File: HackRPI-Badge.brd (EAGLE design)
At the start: 101.6 x 71.1 mm, 24 parts, among them IC1 74595, IC2 74595, IC3 74595

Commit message: Moved resistor nets to ensure constant LED brightness, added serial connector, added 74HC165 for input
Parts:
- removed R7: 10k, SparkFun-Resistors:0603-RES
- removed R8: 470, SparkFun-Resistors:0603-RES
- removed RESET: (no value), SparkFun-Electromechanical:TACTILE-SWITCH-SMD
- added C5: .1uF, SparkFun-Capacitors:0603-CAP
- added J1: FTDI_BASICPTH, SparkFun-Connectors:FTDI_BASIC
- added J2: SOLDERJUMPERTRACE-PTH, SparkFun-Retired:SJ_2S-TRACE-PTH
- added RN1, RN2, RN3, RN4: 47, SparkFun-Passives:0603-ARV
- added U$1: 74165DT, mylib:TSSOP16
- R2, R3: value 47 -> 10k; device SparkFun-Passives:0603-ARV -> SparkFun-Resistors:0603-RES
- R6: value 10k -> 470
- moved R2 24.2 mm to (-50.8, -38.1)
- moved R3 21.6 mm to (-50.8, -41.9)
- moved R5 14.0 mm to (-50.8, -55.9)
- moved R6 14.0 mm to (-50.8, -59.7)
- moved R4 7.62 mm to (-50.8, -45.7)
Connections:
- new net DTR: C5.2, J1.DTR
- new net N$1: J2.1, R6.2
- new net N$10: LED_LEFT.6, RN2.1
- new net N$11: LED_LEFT.11, RN2.2
- new net N$3: LED_LEFT.13, RN1.1
- new net N$4: LED_LEFT.3, RN1.2
- new net N$8: LED_LEFT.4, RN1.3
- new net N$9: LED_LEFT.10, RN1.4
- new net RXI: J1.TXO, WIFI.15
- new net TXO: J1.RXI, WIFI.16
- new net VCC: U$1.16
- net 3.3V: now also R3.2, R4.2; no longer R6.2, R7.2
- net C0: now also RN1.8; no longer LED_LEFT.13
- net C1: now also RN1.7; no longer LED_LEFT.3
- net C10: now also RN3.6; no longer LEF_RIGHT.4
- net C11: now also RN3.5; no longer LEF_RIGHT.10
- net C12: now also RN4.8; no longer LEF_RIGHT.6
- net C13: now also RN4.7; no longer LEF_RIGHT.11
- net C14: now also RN4.6; no longer LEF_RIGHT.15
- net C15: now also RN4.5; no longer LEF_RIGHT.16
- net C2: now also RN1.6; no longer LED_LEFT.4
- net C3: now also RN1.5; no longer LED_LEFT.10
- net C4: now also RN2.8; no longer LED_LEFT.6
- net C5: now also RN2.7; no longer LED_LEFT.11
- net C6: now also RN2.6; no longer LED_LEFT.15
- net C7: now also RN2.5; no longer LED_LEFT.16
- net C8: now also RN3.8; no longer LEF_RIGHT.13
- net C9: now also RN3.7; no longer LEF_RIGHT.3
- net GND: now also J1.GND, R2.2, U$1.8; no longer R4.2, RESET.1
- net GPIO0: now also R3.1; no longer R5.1
- net GPIO15: now also R2.1; no longer R4.1
- net GPIO16: now also J2.2; no longer R8.2
- net GPIO2: now also R4.1; no longer R6.1
- net N$12: now also LED_LEFT.15, RN2.3; no longer WIFI.15
- net N$13: now also LED_LEFT.16, RN2.4; no longer WIFI.16
- net N$14: now also ULN1.17; no longer R2.7
- net N$15: now also ULN1.16; no longer R2.6
- net N$16: now also ULN1.15; no longer R2.5
- net N$17: now also ULN1.14; no longer R3.8
- net N$18: now also ULN1.13; no longer R3.7
- net N$19: now also ULN1.12; no longer R3.6
- net N$20: now also ULN1.11; no longer R3.5
- net N$23: now also LEF_RIGHT.13, RN3.1; no longer R2.1, ULN1.18
- net N$24: now also LEF_RIGHT.3, RN3.2; no longer R2.2, ULN1.17
- net N$25: now also LEF_RIGHT.4, RN3.3; no longer R2.3, ULN1.16
- net N$26: now also LEF_RIGHT.10, RN3.4; no longer R2.4, ULN1.15
- net N$27: now also LEF_RIGHT.6, RN4.1; no longer R3.1, ULN1.14
- net N$28: now also LEF_RIGHT.11, RN4.2; no longer R3.2, ULN1.13
- net N$29: now also LEF_RIGHT.15, RN4.3; no longer R3.3, ULN1.12
- net N$30: now also LEF_RIGHT.16, RN4.4; no longer R3.4, ULN1.11
- net N$7: now also ULN1.18; no longer R2.8
- net RESET: now also C5.1, R5.1, R6.1; no longer R7.1, R8.1, RESET.3

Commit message: Updated part names, misc work
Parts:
- added RN5, RN6: 10k, SparkFun-Passives:0603-ARV
- added S1, S2, S3, S4, S5, S6: SWITCH-MOMENTARY-2PTH, SparkFun-Electromechanical:TACTILE-PTH
- renumbered IC1 to U4, IC2 to U5, IC3 to U6, REG to U2, U$1 to U7, ULN1 to U3, WIFI to U1
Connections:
- removed net VCC: U7.16
- new net A: RN5.1, S1.3, U7.11
- new net B: RN5.2, S2.3, U7.12
- new net CLK: U7.2
- new net DOWN: RN6.2, S6.3, U7.4
- new net LEFT: RN5.3, S3.3, U7.13
- new net RIGHT: RN6.1, S5.3, U7.3
- new net UP: RN5.4, S4.3, U7.14
- net 3.3V: now also RN5.5, RN5.6, RN5.7, RN5.8, RN6.7, RN6.8, U7.16
- net GND: now also S1.1, S2.1, S3.1, S4.1, S5.1, S6.1, U7.5, U7.6
- net MISO: now also U7.9
- net OE: now also U7.15

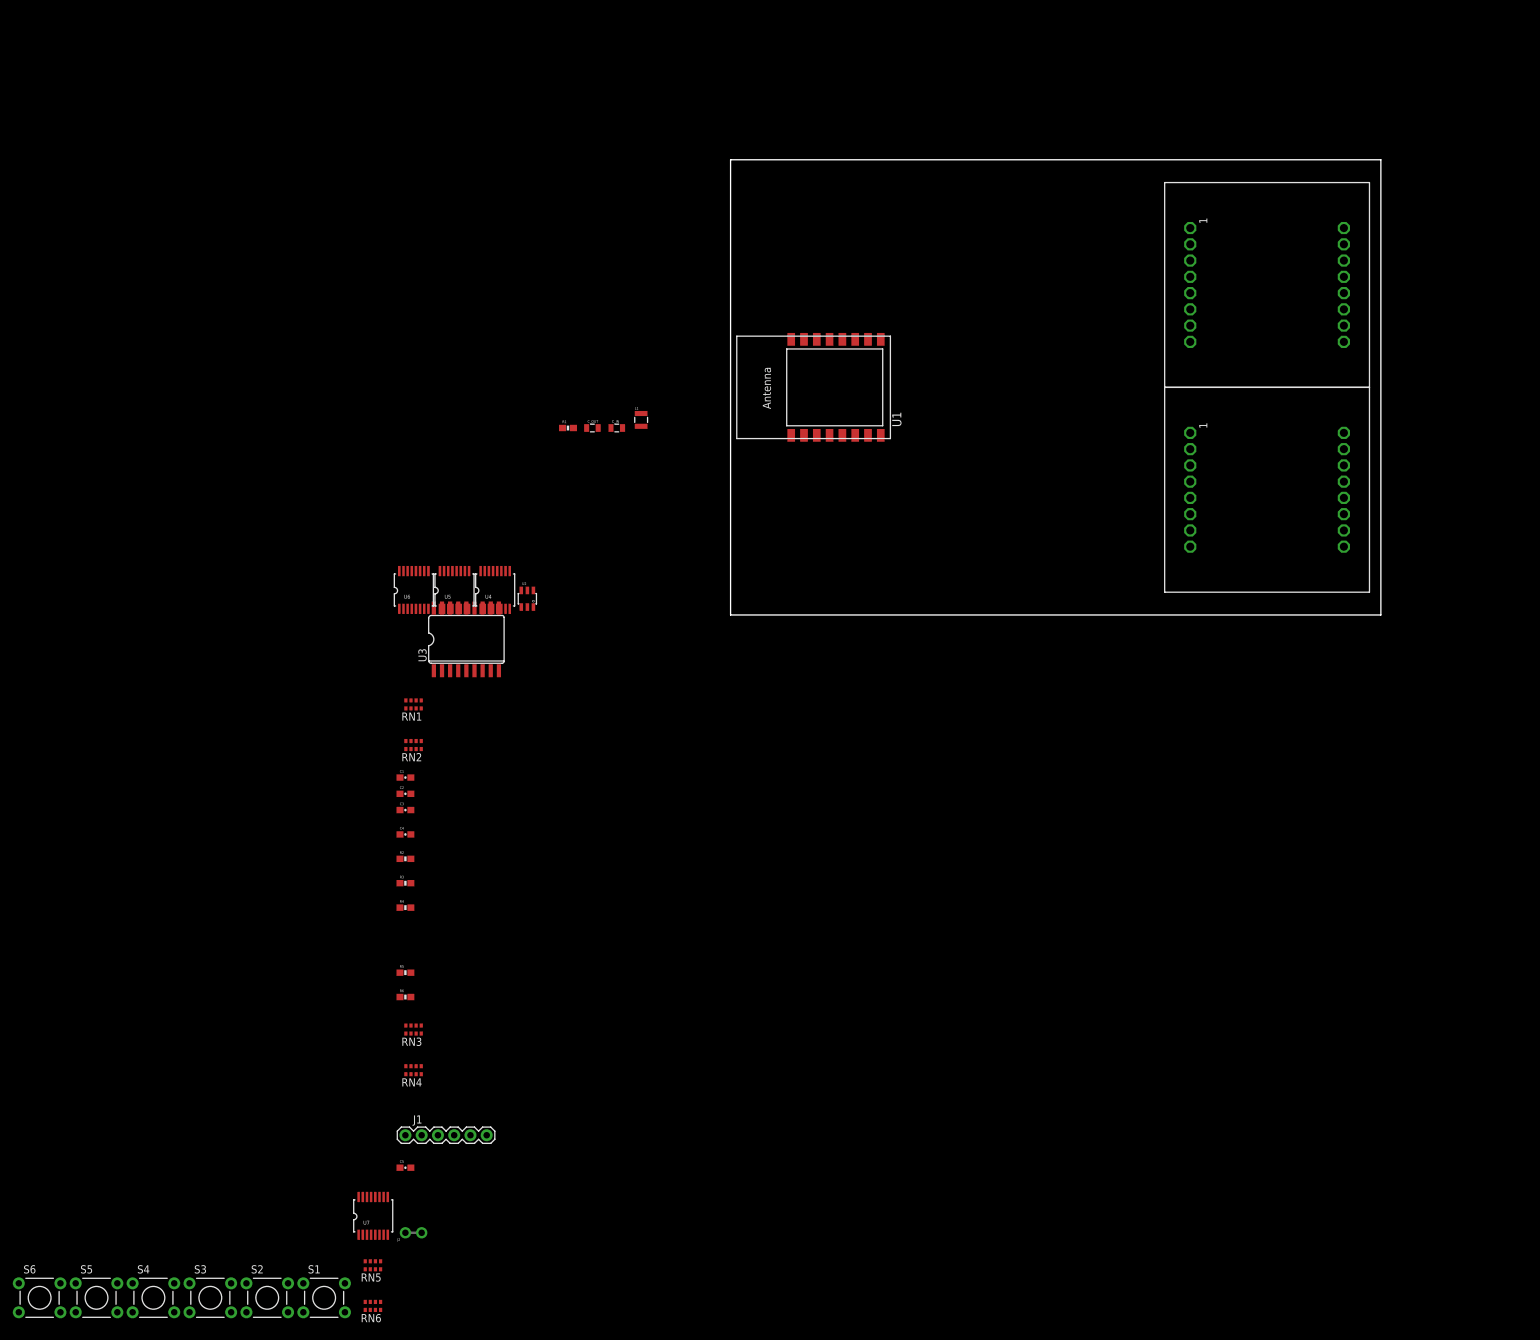
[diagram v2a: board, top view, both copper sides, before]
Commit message: Placed components on board, routed LED matrices and output shift registers, rounded corners of board
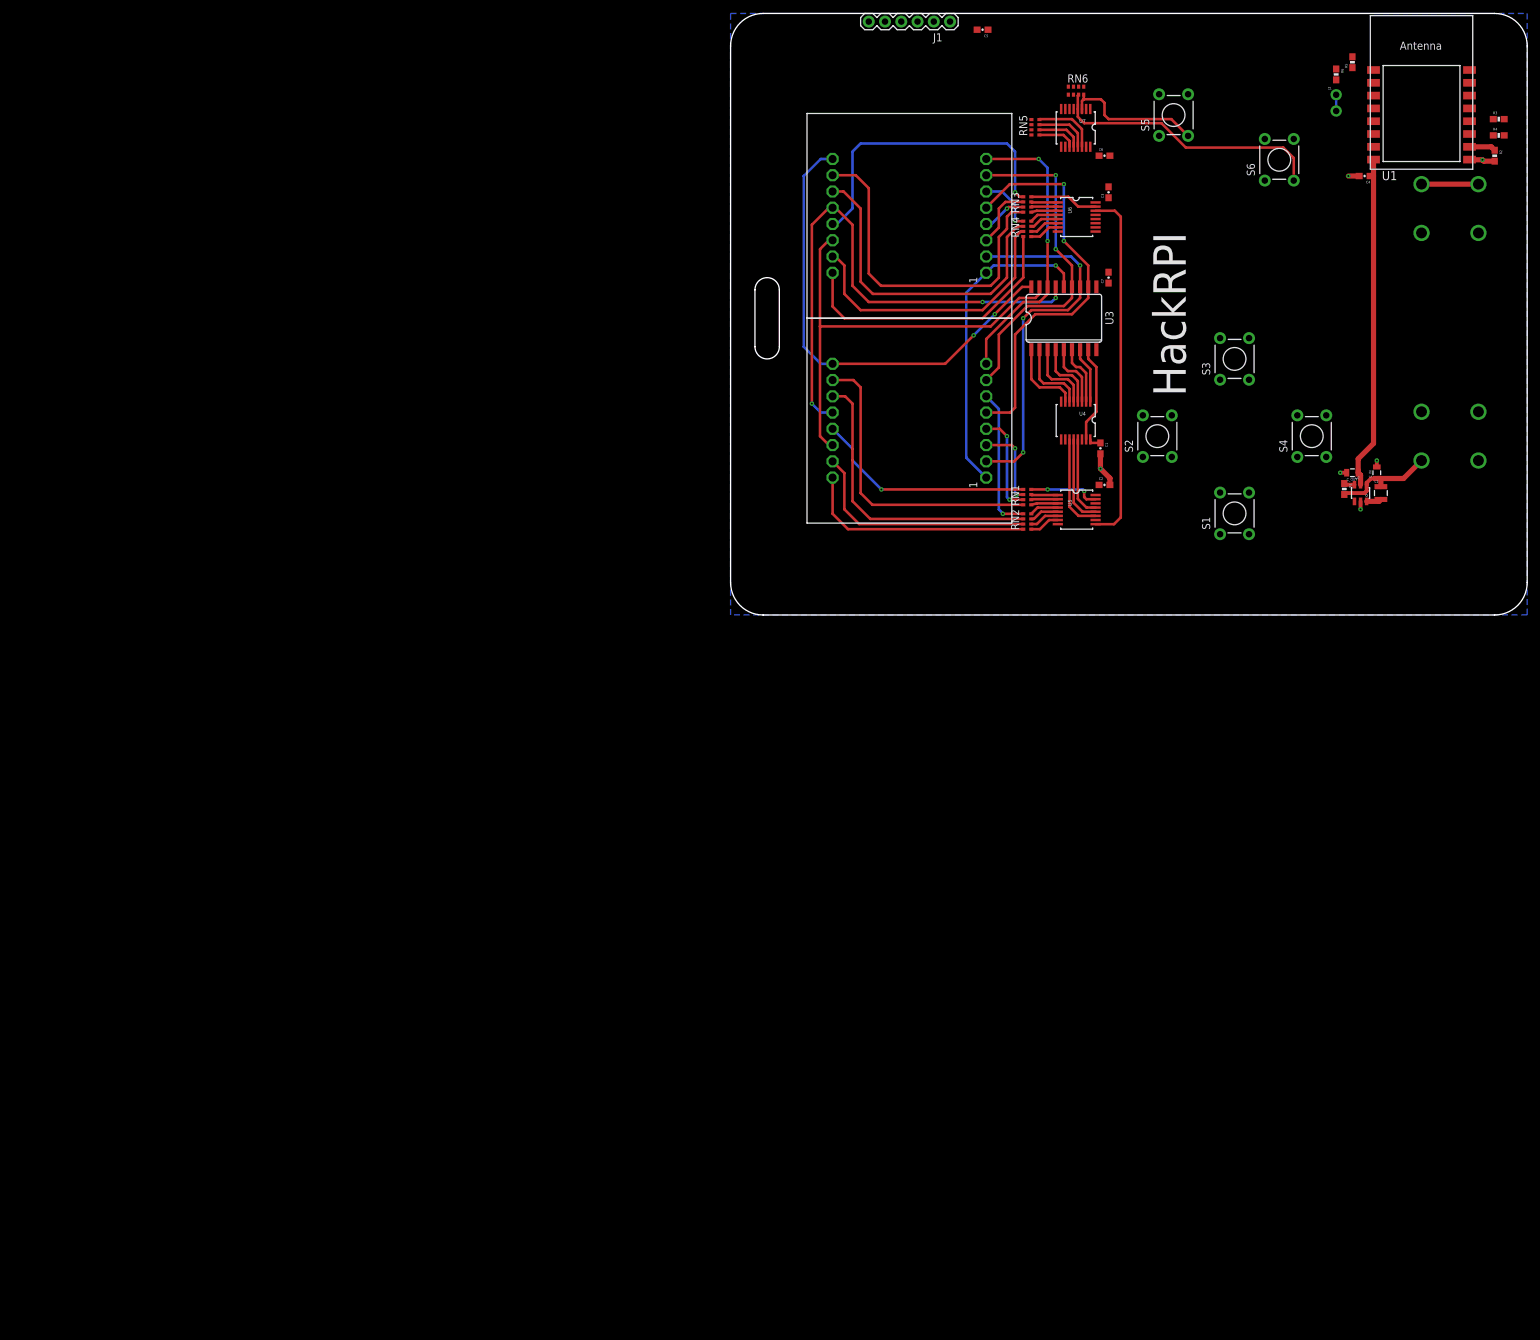
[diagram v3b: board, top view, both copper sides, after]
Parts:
- added BAT1, BAT2: (no value), SparkFun-Electromechanical:BATTERY-AAA
- added C6, C7: .1uF, SparkFun-Capacitors:0603-CAP
- moved S6 262.9 mm to (85.7, 71.1), turned to 90 degrees
- moved S5 249.9 mm to (69.2, 78.1), turned to 90 degrees
- moved J2 227.9 mm to (94.6, 80.0), turned to 270 degrees
- moved S4 225.6 mm to (90.8, 27.9), turned to 90 degrees
- moved RN6 219.4 mm to (54.0, 81.9), turned to 180 degrees
- moved S3 217.1 mm to (78.7, 40.0), turned to 90 degrees
- moved R4 209.1 mm to (120.0, 74.9)
- moved R3 208.4 mm to (120.0, 77.5)
- moved RN5 205.7 mm to (47.6, 76.2), turned to 270 degrees
- moved R5 205.2 mm to (97.2, 86.4), turned to 90 degrees
- moved R6 204.8 mm to (94.6, 84.5), turned to 270 degrees
- moved R2 202.6 mm to (119.4, 71.8), turned to 270 degrees
- moved U7 202.6 mm to (54.0, 76.2), turned to 180 degrees
- moved C5 199.4 mm to (39.4, 91.4), turned to 180 degrees
- moved J1 193.7 mm to (34.3, 92.7), turned to 180 degrees
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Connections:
- new net N$31: BAT1.GND@1, BAT2.PWR@1
- net 3.3V: now also C6.1, C7.1, RN5.1, RN5.2, RN5.3, RN5.4, RN6.1, RN6.2, RN6.3, RN6.4; no longer RN5.5, RN5.6, RN5.7, RN5.8, RN6.7, RN6.8
- net A: now also RN6.8, S5.3, U7.3; no longer RN5.1, S1.3, U7.11
- net B: now also RN6.7, S6.3, U7.4; no longer RN5.2, S2.3, U7.12
- net DOWN: now also RN5.8, S4.3, U7.14; no longer RN6.2, S6.3, U7.4
- net GND: now also BAT2.GND@1, C6.2, C7.2
- net GPIO0: now also U7.1
- net GPIO2: now also U7.15
- net LEFT: now also RN5.5, S1.3, U7.11; no longer RN5.3, S3.3, U7.13
- net OE: no longer U7.15
- net R0: now also U3.8; no longer U3.1
- net R1: now also U3.7; no longer U3.2
- net R2: now also U3.6; no longer U3.3
- net R3: now also U3.5; no longer U3.4
- net R4: now also U3.4; no longer U3.5
- net R5: now also U3.3; no longer U3.6
- net R6: now also U3.2; no longer U3.7
- net R7: now also U3.1; no longer U3.8
- net RIGHT: now also RN5.7, S3.3, U7.13; no longer RN6.1, S5.3, U7.3
- net UP: now also RN5.6, S2.3, U7.12; no longer RN5.4, S4.3, U7.14
- net V_BATT: now also BAT1.PWR@1
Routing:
- net N$16: track 0.00 -> 84.6 mm, vias 0 -> 3
- net N$7: track 0.00 -> 73.9 mm, vias 0 -> 2
- net N$14: track 0.00 -> 71.8 mm
- net N$20: track 0.00 -> 63.1 mm, vias 0 -> 2
- net N$19: track 0.00 -> 57.8 mm, vias 0 -> 3
- net N$22: track 0.00 -> 55.7 mm
- net 3.3V: track 0.00 -> 54.6 mm
- net N$26: track 0.00 -> 54.4 mm
- net N$18: track 0.00 -> 52.8 mm, vias 0 -> 2
- net N$28: track 0.00 -> 51.2 mm
- net N$17: track 0.00 -> 49.8 mm, vias 0 -> 1
- net N$9: track 0.00 -> 47.5 mm
- net N$23: track 0.00 -> 47.4 mm, vias 0 -> 1
- net N$11: track 0.00 -> 46.7 mm
- net N$15: track 0.00 -> 46.2 mm, vias 0 -> 2
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- added copper zone on layer 16, net GND
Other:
- board size 101.6 x 71.1 mm -> 124.5 x 94 mm
- board text added: "HackRPI"

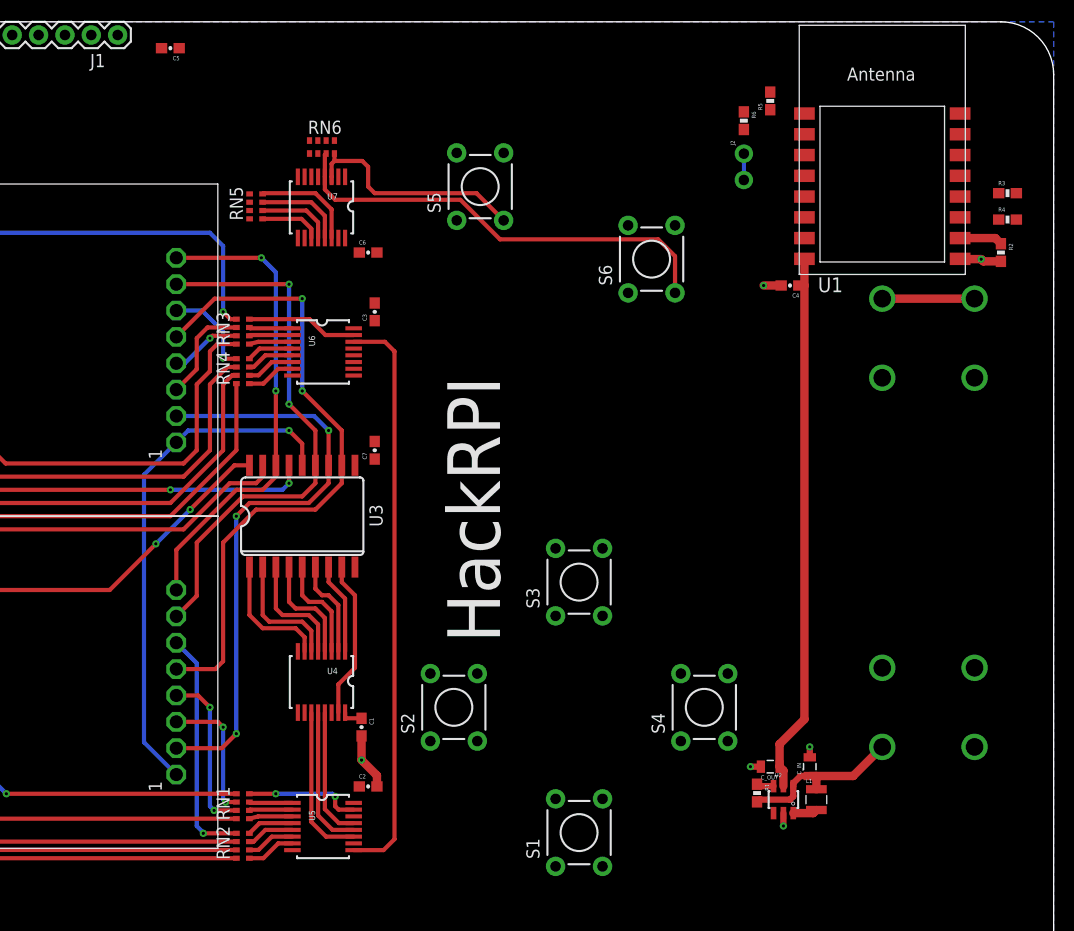
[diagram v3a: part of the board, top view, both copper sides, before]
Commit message: Finished laying out/routing first revision of board
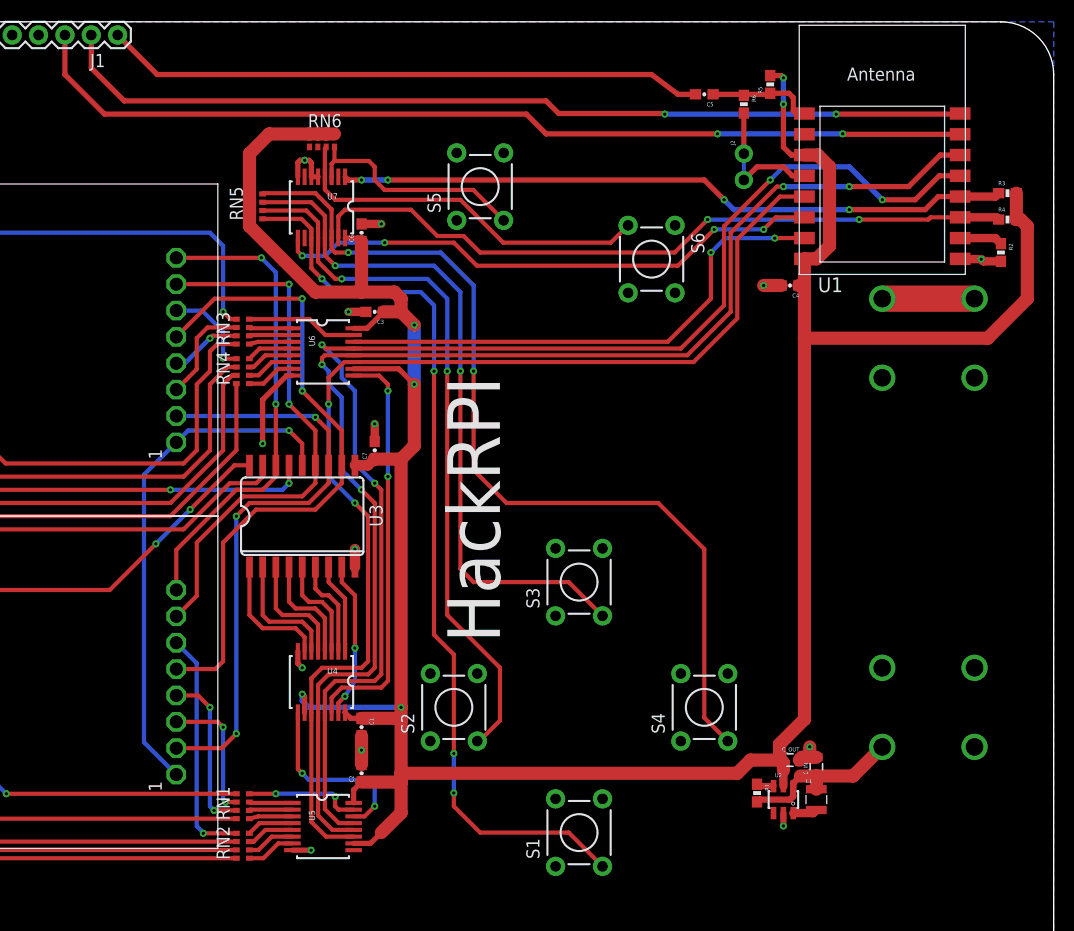
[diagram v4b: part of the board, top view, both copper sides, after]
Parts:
- moved C5 51.6 mm to (90.8, 87.0)
- moved C6 2.01 mm to (57.8, 73.7), turned to 90 degrees
- moved C_OUT 2.01 mm to (99.1, 22.9), turned to 0 degrees
- moved R5 1.59 mm to (97.2, 87.9)
- moved R6 1.59 mm to (94.6, 86.0)
- moved C2 1.42 mm to (57.8, 21.6), turned to 90 degrees
- moved C_IN 0.63 mm to (101.6, 22.2)
- moved RN6 0.63 mm to (54.0, 82.5)
- turned C3 to 180 degrees
- turned S6 to 270 degrees
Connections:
- new net N$33: U5.9
- net MOSI: now also U6.14; no longer U4.14
- net N$22: now also U4.14, U6.9; no longer U5.9, U6.14
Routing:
- net 3.3V: track 54.6 -> 284.5 mm, vias 0 -> 6
- net OE: track 12.6 -> 130.5 mm, vias 0 -> 4
- net LAT: track 13.9 -> 128.7 mm, vias 0 -> 4
- net SCK: track 15.2 -> 111.1 mm, vias 0 -> 2
- net RXI: track 0.00 -> 92.4 mm, vias 0 -> 2
- net TXO: track 0.00 -> 88.7 mm, vias 0 -> 2
- net LEFT: track 5.99 -> 88.0 mm, vias 0 -> 4
- net DOWN: track 10.1 -> 88.9 mm, vias 0 -> 2
- net GPIO2: track 0.00 -> 69.2 mm, vias 0 -> 2
- net GPIO0: track 0.00 -> 64.9 mm, vias 0 -> 4
- net UP: track 7.34 -> 69.3 mm, vias 0 -> 2
- net RIGHT: track 8.68 -> 67.1 mm, vias 0 -> 2
- net DTR: track 0.00 -> 57.9 mm
- net MISO: track 0.00 -> 53.6 mm, vias 0 -> 4
- net MOSI: track 0.00 -> 50.2 mm, vias 0 -> 2
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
